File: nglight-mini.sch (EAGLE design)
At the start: 25 parts, among them X1 53261-04

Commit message: Minor changes
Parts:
- C2: device rcl:C-EUC1206 -> rcl:CPOL-EUUD-4X5,8
- renumbered X1 to I2C
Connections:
- net +5V: now also C2.+; no longer C2.1
- net GND: now also C2.-; no longer C2.2

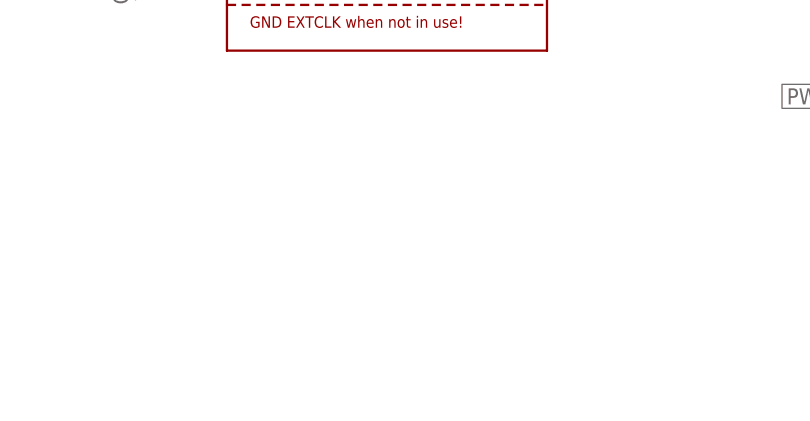
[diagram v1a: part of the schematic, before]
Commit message: Ground unused array resistors
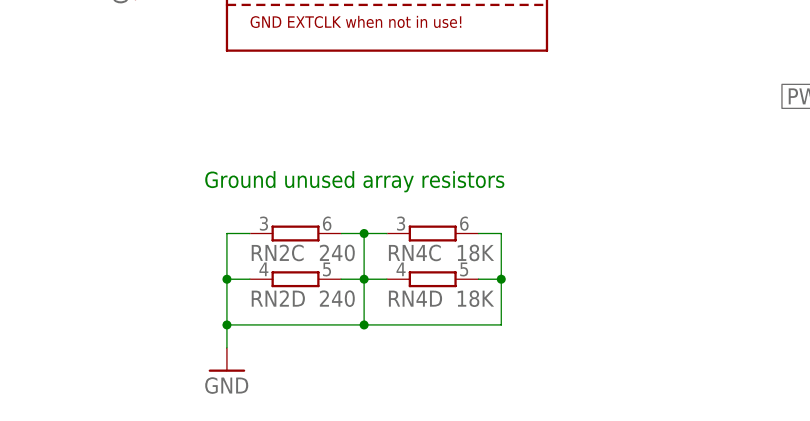
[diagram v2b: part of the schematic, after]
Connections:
- net GND: now also RN2C.1, RN2C.2, RN2D.1, RN2D.2, RN4C.1, RN4C.2, RN4D.1, RN4D.2
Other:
- note added: "Ground unused array resistors"

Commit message: Rev 1; various small improvements, incl.:
- bigger traces (6 mil -> 10 mil)
- larger footprint for the big cap
- remove a small piece of trace between two pins
  that wasn't supposed to be there
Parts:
- C2: device rcl:CPOL-EUUD-4X5,8 -> rcl:CPOL-EUUD-5X5,8
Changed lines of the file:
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@@
 <grid distance="0.1" unitdist="inch" unit="inch" style="lines" multiple="1" display="no" altdistance="0.01" altunitdist="inch" altunit="inch"/>
 <layers>
-<layer number="1" name="Top" color="4" fill="1" visible="no" active="no"/>
-<layer number="2" name="Route2" color="1" fill="3" visible="no" active="no"/>
-<layer number="3" name="Route3" color="4" fill="3" visible="no" active="no"/>
-<layer number="4" name="Route4" color="1" fill="4" visible="no" active="no"/>
-<layer number="5" name="Route5" color="4" fill="4" visible="no" active="no"/>
-<layer number="6" name="Route6" color="1" fill="8" visible="no" active="no"/>
-<layer number="7" name="Route7" color="4" fill="8" visible="no" active="no"/>
-<layer number="8" name="Route8" color="1" fill="2" visible="no" active="no"/>
-<layer number="9" name="Route9" color="4" fill="2" visible="no" active="no"/>
-<layer number="10" name="Route10" color="1" fill="7" visible="no" active="no"/>
-<layer number="11" name="Route11" color="4" fill="7" visible="no" active="no"/>
-<layer number="12" name="Route12" color="1" fill="5" visible="no" active="no"/>
-<layer number="13" name="Route13" color="4" fill="5" visible="no" active="no"/>
-<layer number="14" name="Route14" color="1" fill="6" visible="no" active="no"/>
-<layer number="15" name="Route15" color="4" fill="6" visible="no" active="no"/>
-<layer number="16" name="Bottom" color="1" fill="1" visible="no" active="no"/>
-<layer number="17" name="Pads" color="2" fill="1" visible="no" active="no"/>
-<layer number="18" name="Vias" color="2" fill="1" visible="no" active="no"/>
-<layer number="19" name="Unrouted" color="6" fill="1" visible="no" active="no"/>
-<layer number="20" name="Dimension" color="15" fill="1" visible="no" active="no"/>
-<layer number="21" name="tPlace" color="7" fill="1" visible="no" active="no"/>
-<layer number="22" name="bPlace" color="7" fill="1" visible="no" active="no"/>
-<layer number="23" name="tOrigins" color="15" fill="1" visible="no" active="no"/>
-<layer number="24" name="bOrigins" color="15" fill="1" visible="no" active="no"/>
-<layer number="25" name="tNames" color="7" fill="1" visible="no" active="no"/>
-<layer number="26" name="bNames" color="7" fill="1" visible="no" active="no"/>
-<layer number="27" name="tValues" color="7" fill="1" visible="no" active="no"/>
-<layer number="28" name="bValues" color="7" fill="1" visible="no" active="no"/>
+<layer number="1" name="Top" color="4" fill="1" visible="yes" active="no"/>
+<layer number="2" name="Route2" color="1" fill="3" visible="yes" active="no"/>
+<layer number="3" name="Route3" color="4" fill="3" visible="yes" active="no"/>
+<layer number="4" name="Route4" color="1" fill="4" visible="yes" active="no"/>
+<layer number="5" name="Route5" color="4" fill="4" visible="yes" active="no"/>
+<layer number="6" name="Route6" color="1" fill="8" visible="yes" active="no"/>
+<layer number="7" name="Route7" color="4" fill="8" visible="yes" active="no"/>
+<layer number="8" name="Route8" color="1" fill="2" visible="yes" active="no"/>
+<layer number="9" name="Route9" color="4" fill="2" visible="yes" active="no"/>
+<layer number="10" name="Route10" color="1" fill="7" visible="yes" active="no"/>
+<layer number="11" name="Route11" color="4" fill="7" visible="yes" active="no"/>
+<layer number="12" name="Route12" color="1" fill="5" visible="yes" active="no"/>
+<layer number="13" name="Route13" color="4" fill="5" visible="yes" active="no"/>
+<layer number="14" name="Route14" color="1" fill="6" visible="yes" active="no"/>
+<layer number="15" name="Route15" color="4" fill="6" visible="yes" active="no"/>
+<layer number="16" name="Bottom" color="1" fill="1" visible="yes" active="no"/>
+<layer number="17" name="Pads" color="2" fill="1" visible="yes" active="no"/>
+<layer number="18" name="Vias" color="2" fill="1" visible="yes" active="no"/>
+<layer number="19" name="Unrouted" color="6" fill="1" visible="yes" active="no"/>
+<layer number="20" name="Dimension" color="15" fill="1" visible="yes" active="no"/>
+<layer number="21" name="tPlace" color="7" fill="1" visible="yes" active="no"/>
+<layer number="22" name="bPlace" color="7" fill="1" visible="yes" active="no"/>
+<layer number="23" name="tOrigins" color="15" fill="1" visible="yes" active="no"/>
+<layer number="24" name="bOrigins" color="15" fill="1" visible="yes" active="no"/>
+<layer number="25" name="tNames" color="7" fill="1" visible="yes" active="no"/>
+<layer number="26" name="bNames" color="7" fill="1" visible="yes" active="no"/>
+<layer number="27" name="tValues" color="7" fill="1" visible="yes" active="no"/>
+<layer number="28" name="bValues" color="7" fill="1" visible="yes" active="no"/>
 <layer number="29" name="tStop" color="7" fill="3" visible="no" active="no"/>
 <layer number="30" name="bStop" color="7" fill="6" visible="no" active="no"/>
@@
 <layer number="35" name="tGlue" color="7" fill="4" visible="no" active="no"/>
 <layer number="36" name="bGlue" color="7" fill="5" visible="no" active="no"/>
-<layer number="37" name="tTest" color="7" fill="1" visible="no" active="no"/>
-<layer number="38" name="bTest" color="7" fill="1" visible="no" active="no"/>
+<layer number="37" name="tTest" color="7" fill="1" visible="yes" active="no"/>
+<layer number="38" name="bTest" color="7" fill="1" visible="yes" active="no"/>
 <layer number="39" name="tKeepout" color="4" fill="11" visible="no" active="no"/>
 <layer number="40" name="bKeepout" color="1" fill="11" visible="no" active="no"/>
@@
 <layer number="44" name="Drills" color="7" fill="1" visible="no" active="no"/>
 <layer number="45" name="Holes" color="7" fill="1" visible="no" active="no"/>
-<layer number="46" name="Milling" color="3" fill="1" visible="no" active="no"/>
-<layer number="47" name="Measures" color="7" fill="1" visible="no" active="no"/>
-<layer number="48" name="Document" color="7" fill="1" visible="no" active="no"/>
-<layer number="49" name="Reference" color="7" fill="1" visible="no" active="no"/>
-<layer number="50" name="dxf" color="7" fill="1" visible="no" active="no"/>
-<layer number="51" name="tDocu" color="7" fill="1" visible="no" active="no"/>
-<layer number="52" name="bDocu" color="7" fill="1" visible="no" active="no"/>
-<layer number="53" name="tGND_GNDA" color="7" fill="9" visible="no" active="no"/>
-<layer number="54" name="bGND_GNDA" color="1" fill="9" visible="no" active="no"/>
-<layer number="56" name="wert" color="7" fill="1" visible="no" active="no"/>
-<layer number="57" name="tCAD" color="7" fill="1" visible="no" active="no"/>
+<layer number="46" name="Milling" color="3" fill="1" visible="yes" active="no"/>
+<layer number="47" name="Measures" color="7" fill="1" visible="yes" active="no"/>
+<layer number="48" name="Document" color="7" fill="1" visible="yes" active="no"/>
+<layer number="49" name="Reference" color="7" fill="1" visible="yes" active="no"/>
+<layer number="50" name="dxf" color="7" fill="1" visible="yes" active="no"/>
+<layer number="51" name="tDocu" color="7" fill="1" visible="yes" active="no"/>
+<layer number="52" name="bDocu" color="7" fill="1" visible="yes" active="no"/>
+<layer number="53" name="tGND_GNDA" color="7" fill="9" visible="yes" active="no"/>
+<layer number="54" name="bGND_GNDA" color="1" fill="9" visible="yes" active="no"/>
+<layer number="56" name="wert" color="7" fill="1" visible="yes" active="no"/>
+<layer number="57" name="tCAD" color="7" fill="1" visible="yes" active="no"/>
 <layer number="91" name="Nets" color="2" fill="1" visible="yes" active="yes"/>
 <layer number="92" name="Busses" color="1" fill="1" visible="yes" active="yes"/>
@@
 <part name="LED2_PWR" library="wirepad" deviceset="WIREPAD" device="SMD5-1,8"/>
 <part name="C1" library="rcl" deviceset="C-EU" device="C0805"/>
-<part name="C2" library="rcl" deviceset="CPOL-EU" device="UD-4X5,8"/>
+<part name="C2" library="rcl" deviceset="CPOL-EU" device="UD-5X5,8"/>
 <part name="GND6" library="supply1" deviceset="GND" device=""/>
 <part name="P+3" library="supply1" deviceset="+5V" device=""/>

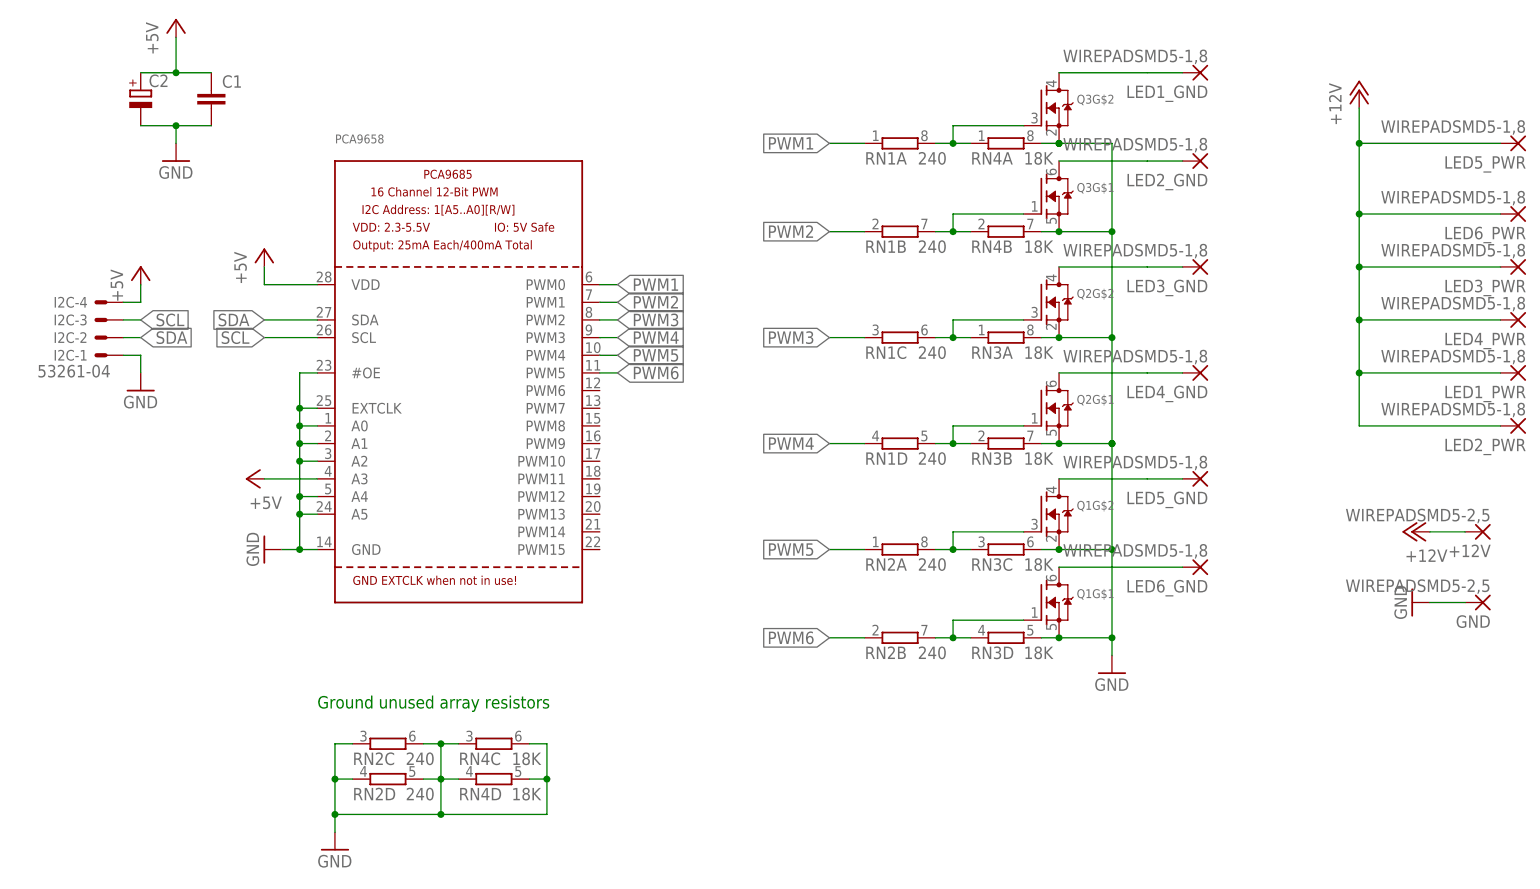
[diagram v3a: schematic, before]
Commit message: Major changes in layout
The resistor arrays proved hard to solder, so I increased
the pad size. Due to the tight space constraints, this led
to relatively big changes in the board. One consequence is
that traces are now 8mil - a compromise between the 6mil
that seemed too fine and the 10mil that just wont fit.
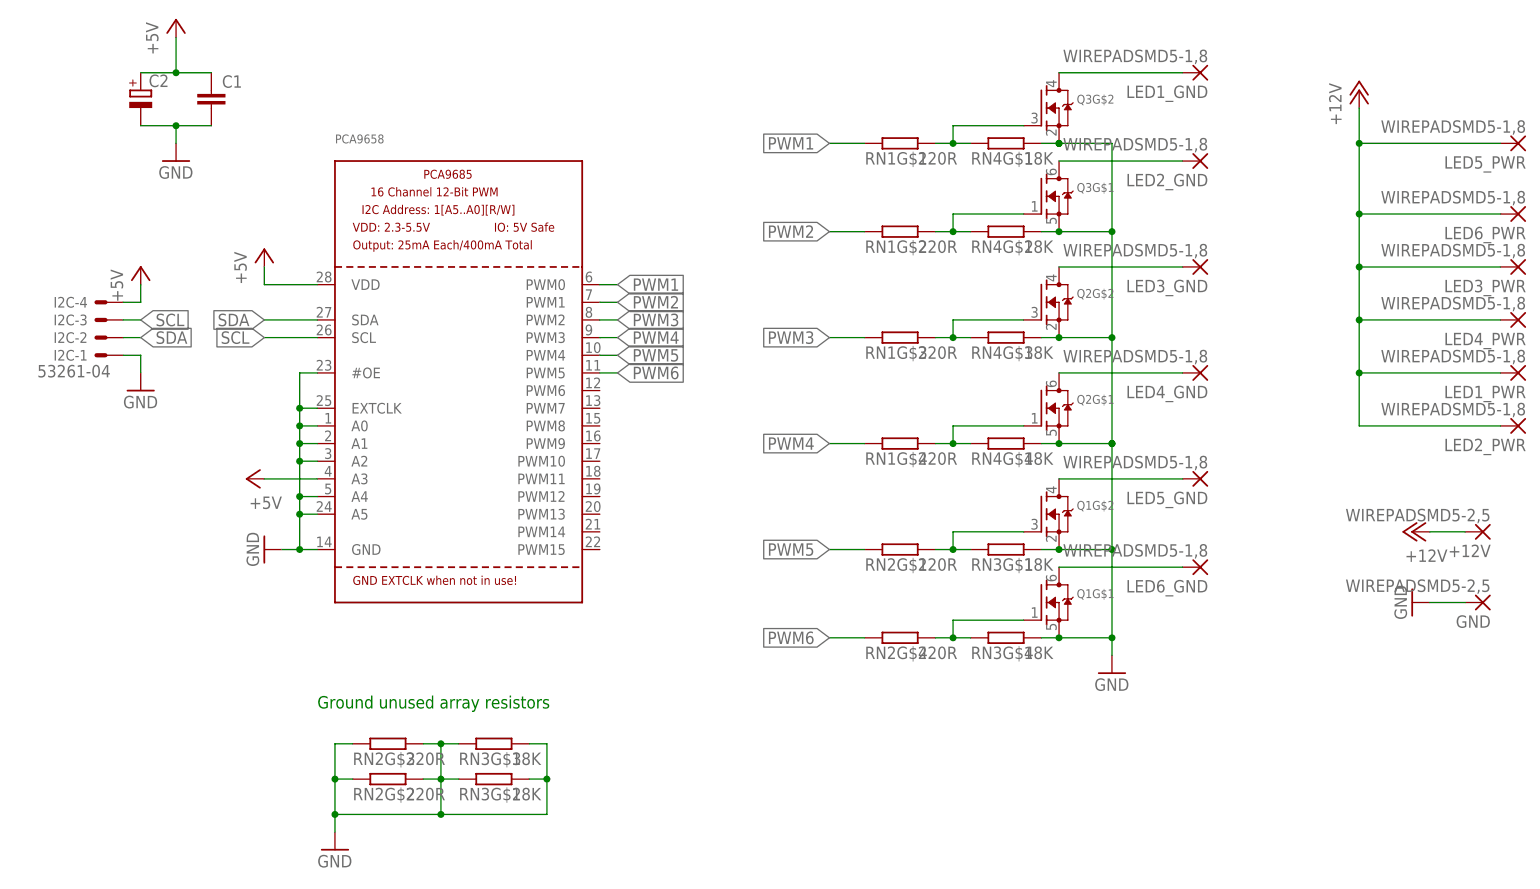
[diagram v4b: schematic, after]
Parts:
- RN1, RN2: value 240 -> 220R; device resistor-dil:4R-N0603-ARC -> r0603array:4_RES_ARRAY; OC_FARNELL unknown -> (none); OC_NEWARK unknown -> (none)
- RN3, RN4: device resistor-dil:4R-N0603-ARC -> r0603array:4_RES_ARRAY; OC_FARNELL unknown -> (none); OC_NEWARK unknown -> (none)
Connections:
- net LED6 renamed N$1
- net GND: now also RN2G$2.P$1, RN2G$2.P$2, RN2G$3.P$1, RN2G$3.P$2, RN3G$1.P$2, RN3G$2.P$1, RN3G$2.P$2, RN3G$3.P$1, RN3G$3.P$2, RN3G$4.P$2, RN4G$1.P$2, RN4G$2.P$2, RN4G$3.P$2, RN4G$4.P$2; no longer RN2C.1, RN2C.2, RN2D.1, RN2D.2, RN3A.2, RN3B.2, RN3C.2, RN3D.2, RN4A.2, RN4B.2, RN4C.1, RN4C.2, RN4D.1, RN4D.2
- net N$11: now also RN1G$2.P$2, RN4G$2.P$1; no longer RN1B.2, RN4B.1
- net N$2: now also RN2G$1.P$2, RN3G$1.P$1; no longer RN2A.2, RN3C.1
- net N$4: now also RN2G$4.P$2, RN3G$4.P$1; no longer RN2B.2, RN3D.1
- net N$6: now also RN1G$3.P$2, RN4G$3.P$1; no longer RN1C.2, RN3A.1
- net N$8: now also RN1G$4.P$2, RN4G$4.P$1; no longer RN1D.2, RN3B.1
- net N$9: now also RN1G$1.P$2, RN4G$1.P$1; no longer RN1A.2, RN4A.1
- net PWM1: now also RN1G$1.P$1; no longer RN1A.1
- net PWM2: now also RN1G$2.P$1; no longer RN1B.1
- net PWM3: now also RN1G$3.P$1; no longer RN1C.1
- net PWM4: now also RN1G$4.P$1; no longer RN1D.1
- net PWM5: now also RN2G$1.P$1; no longer RN2A.1
- net PWM6: now also RN2G$4.P$1; no longer RN2B.1

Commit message: Minor trace/via adjustments
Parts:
- C1: value (none) -> 100n
- C2: value (none) -> 10uF
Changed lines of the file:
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@@
 <part name="LED1_PWR" library="wirepad" deviceset="WIREPAD" device="SMD5-1,8"/>
 <part name="LED2_PWR" library="wirepad" deviceset="WIREPAD" device="SMD5-1,8"/>
-<part name="C1" library="rcl" deviceset="C-EU" device="C0805"/>
-<part name="C2" library="rcl" deviceset="CPOL-EU" device="UD-5X5,8"/>
+<part name="C1" library="rcl" deviceset="C-EU" device="C0805" value="100n"/>
+<part name="C2" library="rcl" deviceset="CPOL-EU" device="UD-5X5,8" value="10uF"/>
 <part name="GND6" library="supply1" deviceset="GND" device=""/>
 <part name="P+3" library="supply1" deviceset="+5V" device=""/>
